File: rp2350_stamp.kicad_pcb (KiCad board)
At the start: 4 copper layers, 25 x 25 mm, 71 parts, among them J1 Conn_West, J2 Conn_North, J3 Conn_South, J4 Conn_East, Q1 BSS84, SW1 SW_RESET, SW2 SW_BOOTSEL, U1 W25Q128JVPIQ, U2 XT4051, U3 AP2112K-3.3, U4 RP235x-A, Y1 XYDBPCNANF-12MHZ

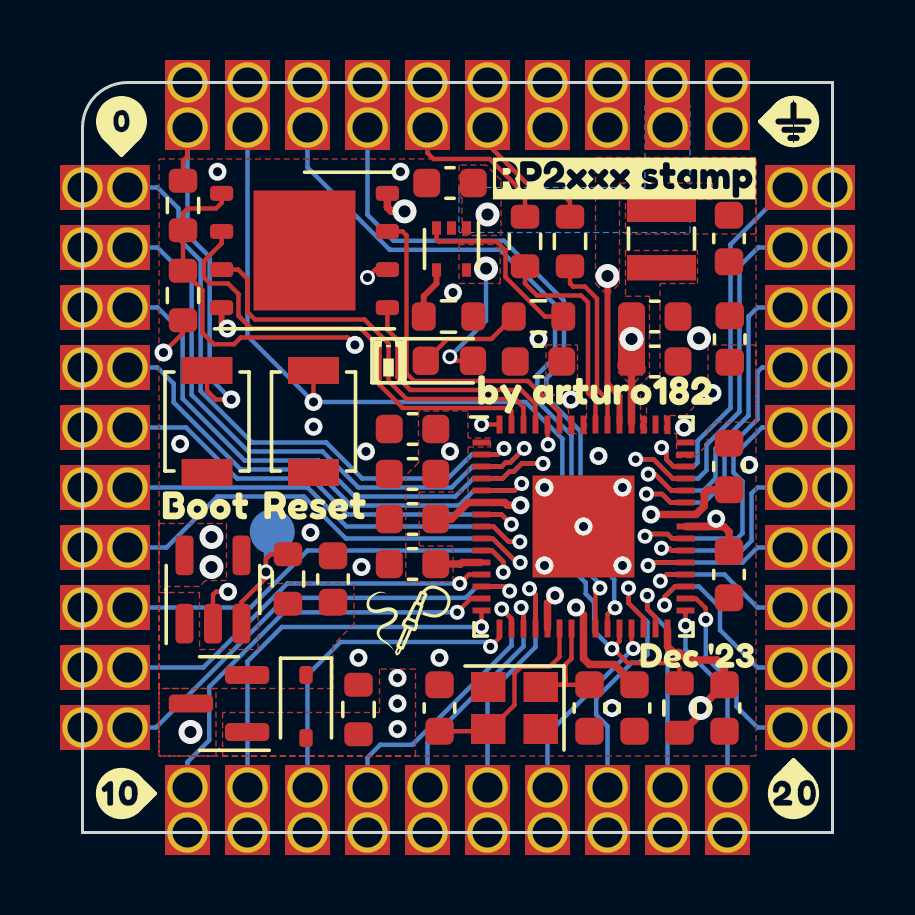
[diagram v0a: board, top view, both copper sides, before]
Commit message: Rev 2
Swapped back to SOT-23 LiPo charger
Added QR Code
Added LDO EN back silk
Moved around front silk
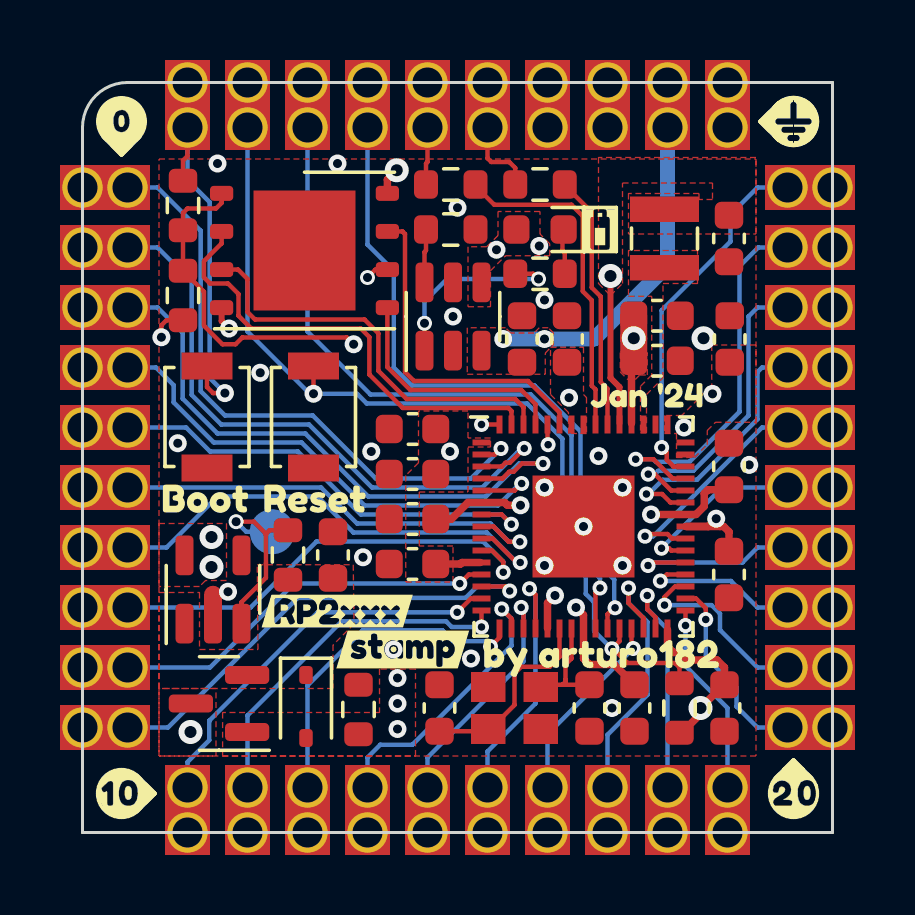
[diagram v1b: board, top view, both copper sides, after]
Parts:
- removed SP-LOGO: LOGO, Symbols_Extra:SolderParty-New-Logo_3x2.5mm_SilkScreen
- removed kibuzzard-6577CB37: G***, kibuzzard-6577CB37
- removed kibuzzard-6579011A: G***, kibuzzard-6579011A
- added G***: LOGO, Symbols_Extra:SolderParty-New-Logo_5x4.2mm_SilkScreen, B.Cu at (149.8, 96.5)
- added G***: LOGO, LOGO, B.Cu at (159.2, 99.3)
- added kibuzzard-65C78BE8: G***, kibuzzard-65C78BE8, F.Cu at (163.8, 95.4)
- added kibuzzard-65C79528: G***, kibuzzard-65C79528, F.Cu at (153.5, 102.6)
- added kibuzzard-65C79539: G***, kibuzzard-65C79539, F.Cu at (155.7, 103.9)
- added kibuzzard-65C80626: G***, kibuzzard-65C80626, B.Cu at (151.3, 104.0)
- U2: value XT4051 -> ME4055; footprint Package_TO_SOT_SMD:SOT-553 -> Package_TO_SOT_SMD:SOT-23-6
- moved kibuzzard-6578FE34 8.78 mm to (162.3, 104.2)
- moved C3 5.73 mm to (159.7, 93.5), turned to -90 degrees
- moved D2 5.32 mm to (160.2, 89.9), turned to 180 degrees
- moved R7 3.12 mm to (157.3, 88.4), turned to 180 degrees
- moved R5 2.90 mm to (157.3, 89.9)
- moved U2 2.25 mm to (157.3, 92.8), turned to 90 degrees
- moved R6 2.15 mm to (160.2, 88.4), turned to 180 degrees
- moved R2 1.43 mm to (160.2, 91.4), turned to 0 degrees
- moved C14 1.21 mm to (161.2, 93.5), turned to 90 degrees
- moved C1 0.80 mm to (153.3, 100.8)
- moved R3 0.80 mm to (151.8, 100.8)
- moved kibuzzard-6577C69C 0.22 mm to (149.1, 98.9)
- moved kibuzzard-6577C6A3 0.22 mm to (152.8, 98.9)
- moved SW1 0.15 mm to (152.7, 96.2)
- moved SW2 0.15 mm to (149.2, 96.2)
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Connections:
- U2 pad 1: VBAT -> Net-(U2-STAT)
- U2 pad 3: Net-(U2-STAT) -> VBAT
- U2 pad 4: Net-(U2-PROG) -> +5V
- U2 pad 5: +5V -> unconnected-(U2-DONE-Pad5)
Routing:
- net VBAT: track 40.7 -> 51.8 mm, vias 2 -> 3
- net +5V: track 46.0 -> 41.3 mm
- net /D+: track 6.87 -> 11.0 mm
- net /USB_D+: track 5.42 -> 1.92 mm
- net /D-: track 5.79 -> 8.32 mm
- net Net-(U3-EN): track 4.42 -> 6.62 mm
- net /GPIO25: track 9.75 -> 7.69 mm
- net Net-(D2-K): track 3.54 -> 1.51 mm
- net /USB_D-: track 4.05 -> 2.63 mm
- net /GPIO29: track 13.3 -> 12.2 mm
- net /GPIO27: track 11.4 -> 10.3 mm
- net /GPIO24: track 6.86 -> 5.87 mm
- net /GPIO28: track 13.8 -> 12.8 mm
- net /GPIO11: track 13.0 -> 12.1 mm
- net /GPIO26: track 9.61 -> 8.79 mm
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- removed copper zone on B.Cu, net VBAT

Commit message: Rev 3
Added a solder jumper for BAT LED
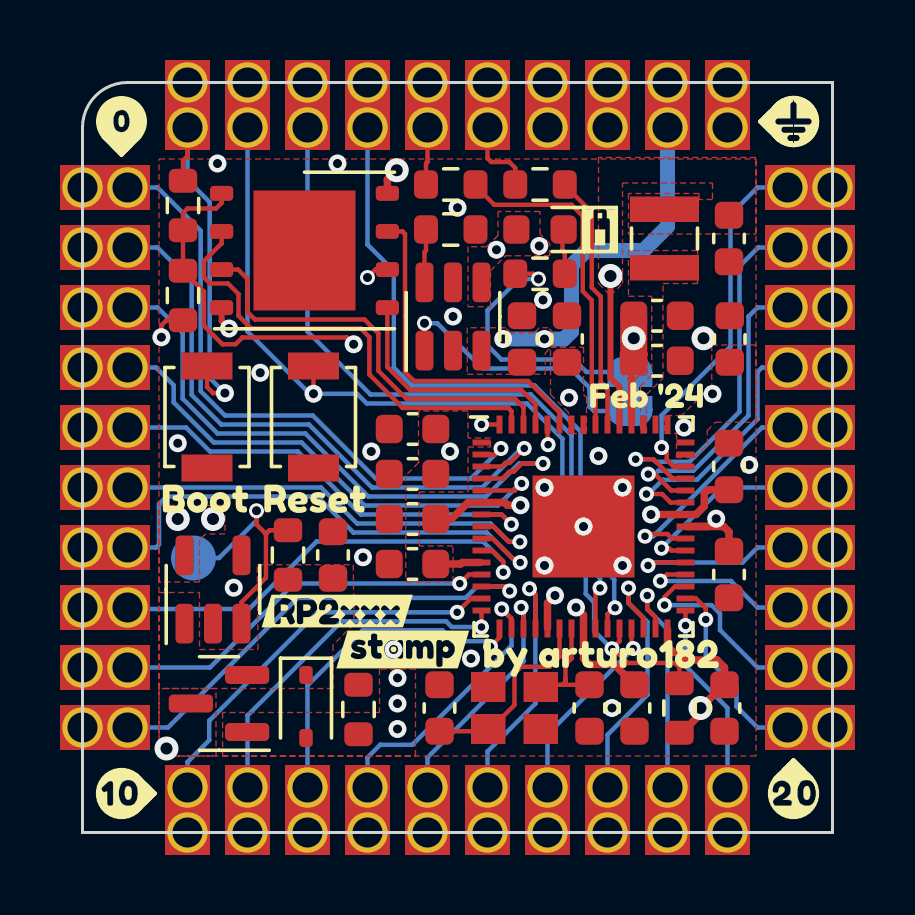
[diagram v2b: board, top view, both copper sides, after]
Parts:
- removed kibuzzard-65C78BE8: G***, kibuzzard-65C78BE8
- removed kibuzzard-65C80626: G***, kibuzzard-65C80626
- added JP1: SJ_STAT_LED, Jumper:SolderJumper-2_P1.3mm_Bridged_RoundedPad1.0x1.5mm, B.Cu at (163.2, 95.3)
- added kibuzzard-6605AA87: G***, kibuzzard-6605AA87, B.Cu at (148.7, 104.2)
- added kibuzzard-6605AAE9: G***, kibuzzard-6605AAE9, B.Cu at (148.7, 106.9)
- added kibuzzard-6605ACF6: G***, kibuzzard-6605ACF6, F.Cu at (163.8, 95.4)
- added kibuzzard-6605B0A1: G***, kibuzzard-6605B0A1, B.Cu at (163.2, 99.7)
- added kibuzzard-6605B0D5: G***, kibuzzard-6605B0D5, B.Cu at (163.2, 102.8)
- moved G*** 17.3 mm to (164.7, 105.4)
- moved G*** 3.20 mm to (156.0, 99.2)
- moved TP1 2.77 mm to (148.7, 100.8)
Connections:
- R2 pad 1: Net-(U2-STAT) -> Net-(JP1-A)
- U2 pad 1: Net-(U2-STAT) -> Net-(JP1-B)
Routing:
- net Net-(JP1-B): track 0.00 -> 8.99 mm, vias 0 -> 1
- net Net-(JP1-A): track 0.00 -> 8.92 mm, vias 0 -> 1
- net Net-(U2-STAT): track 6.60 -> 0.00 mm, vias 2 -> 0
- net GND: track 2.30 -> 0.80 mm
- net Net-(U3-EN): track 6.62 -> 7.96 mm
- net VBAT: track 51.8 -> 53.1 mm
- net /GPIO6: track 16.3 -> 17.1 mm
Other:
- board text added: "0.1uF"
- board text added: "100K"
- board text added: "10uF"
- board text added: "12mHz"
- board text added: "12pF"
- board text added: "1uF"
- board text added: "27R"
- board text added: "2K"
- board text added: "4.7uH"
- board text added: "AP2112K"
- board text added: "BSS84"
- board text added: "LED"
- board text added: "ME4055"
- board text added: "RP235x-A"
- board text added: "Schottky"
- board text added: "W25Q128JVPIQ"

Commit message: Rev 4
- Put chip name on the board
- Fixup pin markers to be uniform
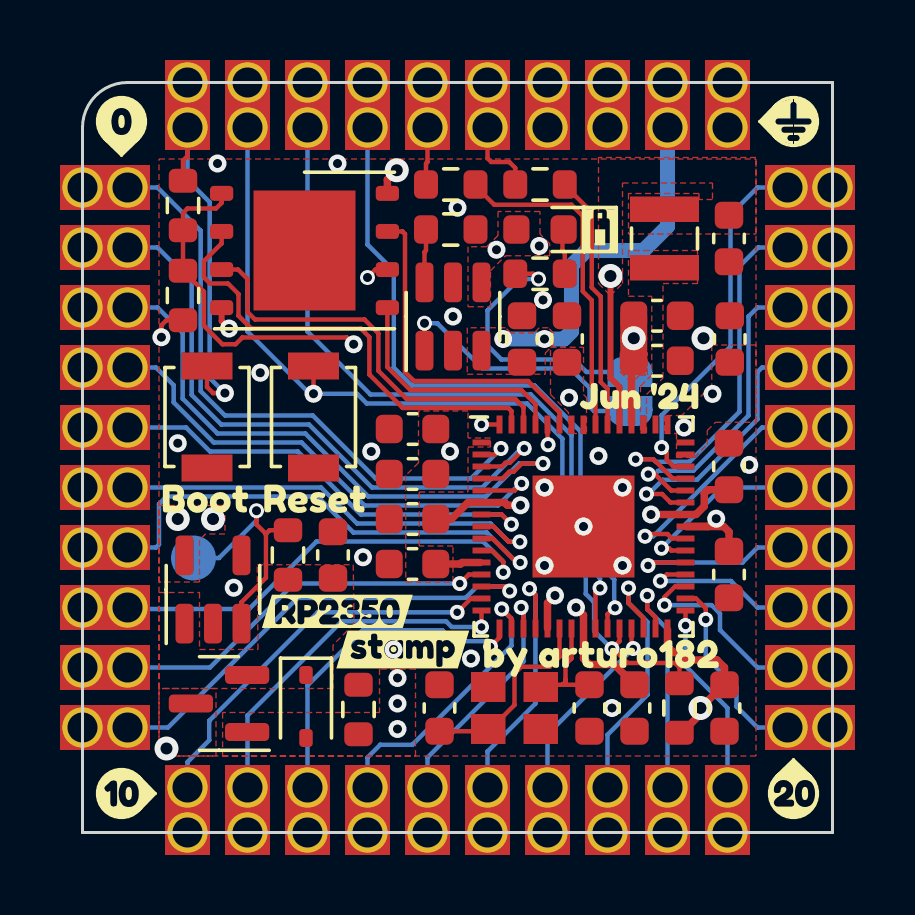
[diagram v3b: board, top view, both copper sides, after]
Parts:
- removed ? (x6): , buzzardLabel
- removed kibuzzard-65C79528: G***, kibuzzard-65C79528
- removed kibuzzard-6605ACF6: G***, kibuzzard-6605ACF6
- removed svg2mod-1, svg2mod-2, svg2mod-21, svg2mod-51, svg2mod-53, svg2mod-54, svg2mod-92: G***, svg2mod
- added kibuzzard-6695A5B8: G***, kibuzzard-6695A5B8, F.Cu at (153.5, 102.6)
- added kibuzzard-6695A66B: G***, kibuzzard-6695A66B, F.Cu at (163.6, 95.5)
- added kibuzzard-6695ACF2: G***, kibuzzard-6695ACF2, F.Cu at (146.3, 108.7)
- added kibuzzard-6695ACF2: G***, kibuzzard-6695ACF2, B.Cu at (146.3, 108.7)
- added kibuzzard-6695AD18: G***, kibuzzard-6695AD18, F.Cu at (146.3, 86.3)
- added kibuzzard-6695AD18: G***, kibuzzard-6695AD18, B.Cu at (146.3, 86.3)
- added kibuzzard-6695AD2C: G***, kibuzzard-6695AD2C, F.Cu at (168.7, 108.7)
- added kibuzzard-6695AD2C: G***, kibuzzard-6695AD2C, B.Cu at (168.7, 108.7)
- added kibuzzard-6695B1B2: G***, kibuzzard-6695B1B2, B.Cu at (168.7, 86.3)
- added kibuzzard-6695B237: G***, kibuzzard-6695B237, B.Cu at (166.3, 96.5)
- added kibuzzard-6695B2B8: G***, kibuzzard-6695B2B8, B.Cu at (158.5, 106.3)
- added kibuzzard-6695B350: G***, kibuzzard-6695B350, B.Cu at (148.7, 98.5)
- U4: value RP235x-A -> RP2350-A
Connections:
- U3 pad 4: unconnected-(U3-NC-Pad4) -> GND

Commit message: Rev 4.5
Fixup power stuff according to RPi's recommendations
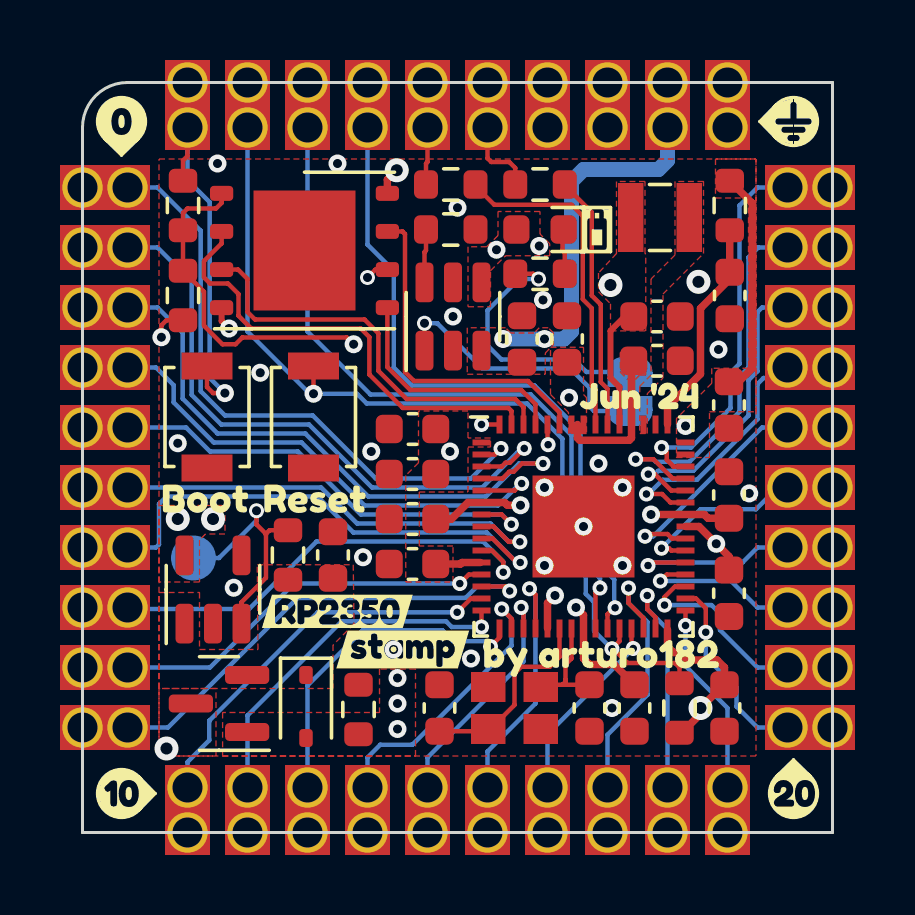
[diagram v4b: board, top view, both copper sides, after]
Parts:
- removed C12: 0.1uF, Capacitor_SMD:C_0603_1608Metric
- added C8: 4.7uF, Capacitor_SMD:C_0603_1608Metric, F.Cu at (166.6, 92.1)
- added R8: 27R, Resistor_SMD:R_0603_1608Metric, F.Cu at (166.6, 89.1)
- C13: value 1uF -> 0.1uF
- C15, C16: value 10uF -> 4.7uF
- L1: value 4.7uH -> 3.3uH
- moved C16 3.54 mm to (164.2, 92.8), turned to 0 degrees
- moved C13 2.20 mm to (166.6, 95.8), turned to -90 degrees
- moved C19 0.95 mm to (166.6, 98.8)
- moved L1 0.72 mm to (164.2, 89.5), turned to 0 degrees
- moved C10 0.62 mm to (166.6, 102.0)
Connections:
- net Net-(U4-VREG_FB) renamed +1.1V
- U3 pad 4: GND -> unconnected-(U3-NC-Pad4)
- U4 pad 46: +3V3 -> Net-(U4-VREG_AVDD)
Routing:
- net +3V3: track 17.2 -> 25.2 mm, vias 12 -> 10
- net Net-(U4-VREG_AVDD): track 0.00 -> 7.33 mm
- net +1.1V: track 30.9 -> 29.2 mm
- net /GPIO29: track 12.2 -> 12.8 mm
- net VBAT: track 53.1 -> 53.6 mm
- net GND: vias 21 -> 22

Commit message: Fix BOM info, add README and LICENSE
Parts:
- U3: value AP2112K-3.3 -> ME6211
- Y1: value XYDBPCNANF-12MHZ -> CM4012M00012001
